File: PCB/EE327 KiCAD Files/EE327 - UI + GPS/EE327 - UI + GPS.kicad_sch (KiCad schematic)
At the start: 0 parts

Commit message: pcb start
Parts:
- added J1: Conn_01x09_Socket, symbol Connector:Conn_01x09_Socket
- added J2: Conn_01x14_Socket, symbol Connector:Conn_01x14_Socket
- added R1, R2: 10k, symbol Device:R
- added SW1, SW2: SW_Push, symbol Switch:SW_Push
- added U1: ESP32-WROOM-32E-N4, symbol EE327 symbols:ESP32-WROOM-32E-N4
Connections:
- new net +3.3V: J1.9 (Pin_9), J2.1 (Pin_1), R1.1, R2.1, U1.2 (3V3)
- new net BOOT: SW2.2, U1.25 (IO0)
- new net ESP_RST: SW1.2, U1.3 (EN)
- new net GND: J1.3 (Pin_3), J2.2 (Pin_2), R1.2, R2.2, SW1.1, SW2.1, U1.1 (GND), U1.38 (GND), U1.39 (GND), U1.40 (GND), U1.41 (GND), U1.42 (GND), U1.43 (GND), U1.44 (GND), U1.45 (GND), U1.46 (GND), U1.47 (GND)
- new net GPS_RX: J1.4 (Pin_4), U1.28 (IO17)
- new net GPS_TX: J1.5 (Pin_5), U1.27 (IO16)
- new net TFT_CS: J2.3 (Pin_3), U1.23 (IO15)
- new net TFT_DC: J2.5 (Pin_5), U1.24 (IO2)
- new net TFT_MOSI: J2.6 (Pin_6), U1.37 (IO23)
- new net TFT_RST: J2.4 (Pin_4), U1.26 (IO4)
- new net TFT_SCK: J2.7 (Pin_7), U1.31 (IO19)

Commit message: pcb
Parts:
- added C1: C, symbol Device:C
- added C5: 1uF, Capacitor_SMD:C_0805_2012Metric, symbol Device:C
- added C6: 4.7uF, Capacitor_SMD:C_0805_2012Metric, symbol Device:C
- added D1, D2: D_Schottky, symbol Device:D_Schottky
- added D4: LED, LED_SMD:LED_0603_1608Metric_Pad1.05x0.95mm_HandSolder, symbol Device:LED
- added J3: Conn_01x06_Pin, symbol Connector:Conn_01x06_Pin
- added J4: Conn_01x04_Socket, symbol Connector:Conn_01x04_Socket
- added J5: Conn_01x02_Socket, symbol Connector:Conn_01x02_Socket
- added R5: 330R, Resistor_SMD:R_0805_2012Metric_Pad1.20x1.40mm_HandSolder, symbol Device:R
- added U3: LDL1117S30R, EE326:voltage regulator, symbol EE326:LDL1117S30R
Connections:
- net +3.3V: now also C1.1, J3.1 (Pin_1)
- net GND: now also C1.2, C5.2, C6.2, D4.1 (K), J3.6 (Pin_6), J4.1 (Pin_1), J5.1 (Pin_1), U3.1 (GND)
- net RX0: now reaches U1.34 (RXD0)
- net RX0: now also J4.2 (Pin_2)
- net TX0: now reaches U1.35 (TXD0)
- net TX0: now also J4.3 (Pin_3)
- new net: D4.2 (A), R5.2
- new net +3V3: C6.1, R5.1, U3.4 (VOUT__1)
- new net LDO_IN: C5.1, D1.1 (K), D2.1 (K), U3.3 (VIN)
- new net L/R: J3.4 (Pin_4)
- new net SCL: J3.3 (Pin_3)
- new net SDA: J3.2 (Pin_2)
- new net Terminal_5V: D2.2 (A), J5.2 (Pin_2)
- new net USB_5V: D1.2 (A), J4.4 (Pin_4)
- new net WS: J3.5 (Pin_5)
- no-connect marks 0 -> 1
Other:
- note added: "Buttons for reset and IO0"
- note added: "GPS module socket"
- note added: "Microphone connector"
- note added: "POWER REGULATOR + LED"
- note added: "Screw terminal power input"
- note added: "TFT_display socket"
- note added: "USB to UART converter output, can power board but mainly to program"
- moved on the sheet: J1, J2, R1, R2, SW1, SW2

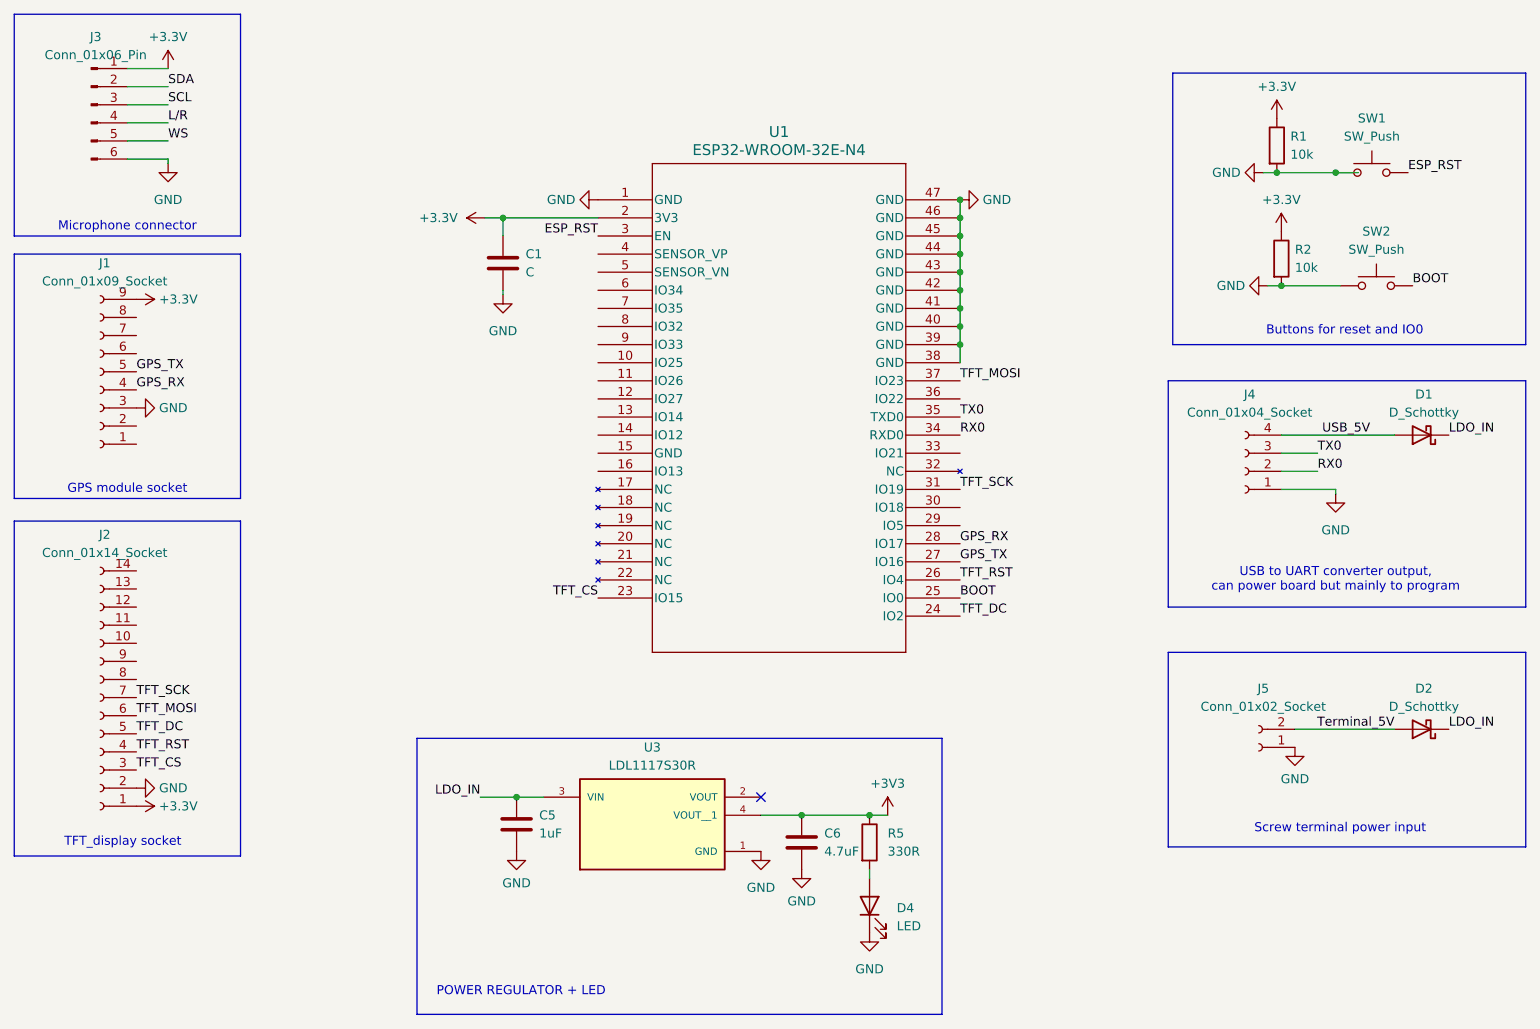
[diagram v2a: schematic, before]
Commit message: Updated user PCB
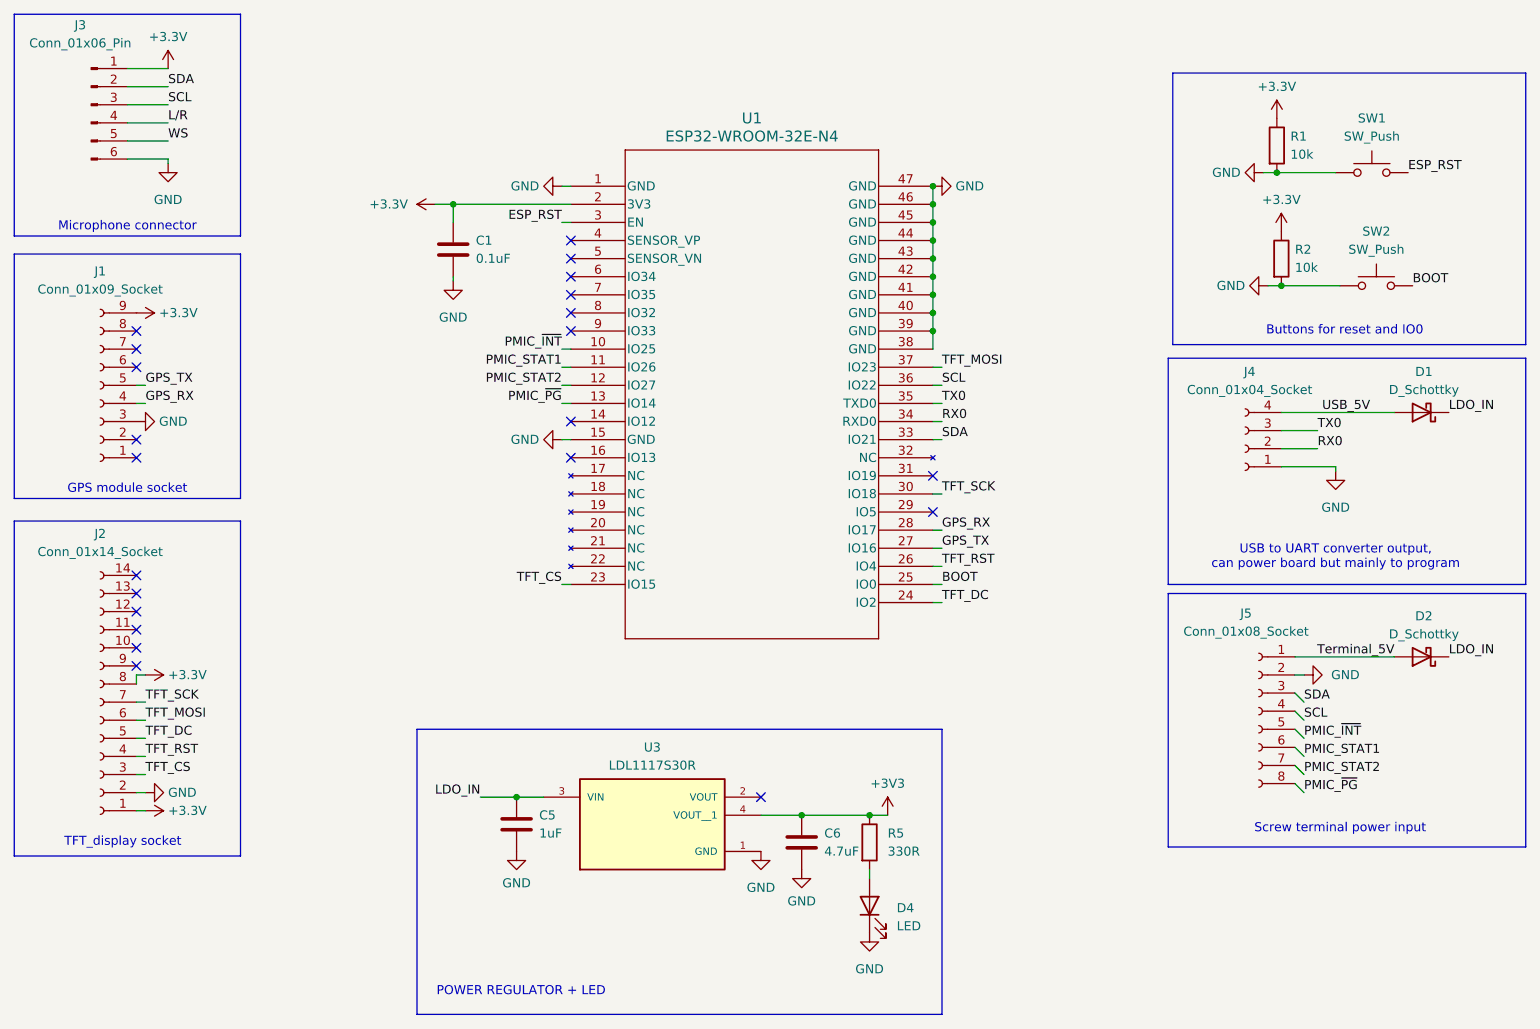
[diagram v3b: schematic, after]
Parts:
- removed J5: Conn_01x02_Socket, symbol Connector:Conn_01x02_Socket
- added J5: Conn_01x08_Socket, symbol Connector:Conn_01x08_Socket
- C1: value C -> 0.1uF
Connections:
- net +3.3V: now also J2.8 (Pin_8)
- net GND: now also U1.15 (GND), J5.2 (Pin_2)
- net SCL: now also U1.36 (IO22), J5.4 (Pin_4)
- net SDA: now also U1.33 (IO21), J5.3 (Pin_3)
- net TFT_SCK: now also U1.30 (IO18); no longer U1.31 (IO19)
- net Terminal_5V: now also J5.1 (Pin_1)
- net PMIC_~{INT}: now reaches U1.10 (IO25)
- net PMIC_~{INT}: now also J5.5 (Pin_5)
- net PMIC_STAT1: now reaches U1.11 (IO26)
- net PMIC_STAT1: now also J5.6 (Pin_6)
- net PMIC_STAT2: now reaches U1.12 (IO27)
- net PMIC_STAT2: now also J5.7 (Pin_7)
- net PMIC_~{PG}: now reaches U1.13 (IO14)
- net PMIC_~{PG}: now also J5.8 (Pin_8)
- no-connect marks 1 -> 22
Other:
- moved on the sheet: C1, D1, D2, J1, J2, J4, U1

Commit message: PCB routing started
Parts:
- C1: footprint (none) -> Capacitor_SMD:C_0805_2012Metric_Pad1.18x1.45mm_HandSolder
- C5, C6: footprint Capacitor_SMD:C_0805_2012Metric -> Capacitor_SMD:C_0805_2012Metric_Pad1.18x1.45mm_HandSolder
- D1, D2: footprint (none) -> EE327_Symbols:Schottky
- J1: footprint (none) -> Connector_PinHeader_2.54mm:PinHeader_1x09_P2.54mm_Vertical
- J2: footprint (none) -> Connector_PinHeader_2.54mm:PinHeader_1x14_P2.54mm_Vertical
- J3: footprint (none) -> EE327_Symbols:1x6 JST
- J4: footprint (none) -> Connector_PinHeader_2.54mm:PinHeader_1x04_P2.54mm_Vertical
- J5: footprint (none) -> EE327_Symbols:CONN_B08B-PNDZS-1_JST
- R1, R2: footprint (none) -> Resistor_SMD:R_0805_2012Metric_Pad1.20x1.40mm_HandSolder
- SW1, SW2: footprint (none) -> EE327_Symbols:pushbutton
- U1: footprint (none) -> EE327_Symbols:ESP32­WROOM­32E_EXP
- U3: footprint EE326:voltage regulator -> EE327_Symbols:Voltage Regulator
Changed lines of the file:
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@@
 			)
 		)
-		(property "Footprint" ""
+		(property "Footprint" "Resistor_SMD:R_0805_2012Metric_Pad1.20x1.40mm_HandSolder"
 			(at 207.772 64.135 90)
 			(hide yes)
@@
 			)
 		)
-		(property "Footprint" ""
+		(property "Footprint" "Connector_PinHeader_2.54mm:PinHeader_1x04_P2.54mm_Vertical"
 			(at 205.105 106.68 0)
 			(hide yes)
@@
 			)
 		)
-		(property "Footprint" ""
+		(property "Footprint" "EE327_Symbols:Schottky"
 			(at 229.87 101.6 0)
 			(hide yes)
@@
 			)
 		)
-		(property "Footprint" ""
+		(property "Footprint" "EE327_Symbols:CONN_B08B-PNDZS-1_JST"
 			(at 207.01 143.51 0)
 			(hide yes)
@@
 			)
 		)
-		(property "Footprint" ""
+		(property "Footprint" "Connector_PinHeader_2.54mm:PinHeader_1x14_P2.54mm_Vertical"
 			(at 44.45 142.24 0)
 			(hide yes)
@@
 			)
 		)
-		(property "Footprint" ""
+		(property "Footprint" "Capacitor_SMD:C_0805_2012Metric_Pad1.18x1.45mm_HandSolder"
 			(at 94.9452 82.55 0)
 			(hide yes)
@@
 			)
 		)
-		(property "Footprint" ""
+		(property "Footprint" "Resistor_SMD:R_0805_2012Metric_Pad1.20x1.40mm_HandSolder"
 			(at 208.407 80.01 90)
 			(hide yes)
@@
 			)
 		)
-		(property "Footprint" "EE326:voltage regulator"
+		(property "Footprint" "EE327_Symbols:Voltage Regulator"
 			(at 121.92 158.115 0)
 			(hide yes)
@@
 			)
 		)
-		(property "Footprint" ""
+		(property "Footprint" "EE327_Symbols:pushbutton"
 			(at 222.885 62.865 0)
 			(hide yes)
@@
 			)
 		)
-		(property "Footprint" ""
+		(property "Footprint" "EE327_Symbols:ESP32­WROOM­32E_EXP"
 			(at 110.49 69.85 0)
 			(hide yes)
@@
 			)
 		)
-		(property "Footprint" ""
+		(property "Footprint" "EE327_Symbols:pushbutton"
 			(at 223.52 78.74 0)
 			(hide yes)
@@
 			)
 		)
-		(property "Footprint" ""
+		(property "Footprint" "EE327_Symbols:1x6 JST"
 			(at 43.18 58.42 0)
 			(hide yes)
@@
 			)
 		)
-		(property "Footprint" "Capacitor_SMD:C_0805_2012Metric"
+		(property "Footprint" "Capacitor_SMD:C_0805_2012Metric_Pad1.18x1.45mm_HandSolder"
 			(at 103.8352 163.195 0)
 			(hide yes)
@@
 			)
 		)
-		(property "Footprint" ""
+		(property "Footprint" "Connector_PinHeader_2.54mm:PinHeader_1x09_P2.54mm_Vertical"
 			(at 44.45 97.79 0)
 			(hide yes)
@@
 			)
 		)
-		(property "Footprint" ""
+		(property "Footprint" "EE327_Symbols:Schottky"
 			(at 229.87 135.89 0)
 			(hide yes)
@@
 			)
 		)
-		(property "Footprint" "Capacitor_SMD:C_0805_2012Metric"
+		(property "Footprint" "Capacitor_SMD:C_0805_2012Metric_Pad1.18x1.45mm_HandSolder"
 			(at 143.8402 165.735 0)
 			(hide yes)

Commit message: pcb done?
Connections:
- net +3V3 is gone; now on net +3.3V: C6.1, R5.1, U3.4 (VOUT__1)
- net BOOT: now also R2.2
- net ESP_RST: now also R1.2
- net GND: no longer R1.2, R2.2
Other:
- moved on the sheet: SW1, SW2
